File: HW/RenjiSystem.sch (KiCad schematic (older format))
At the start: 35 parts

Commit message: フットプリントをトランス以外あてがい
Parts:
- added C6: CP1, Capacitor_THT:CP_Radial_D12.5mm_P5.00mm, symbol Device:CP1
- added H1: MountingHole_Pad_AC100V_HOT, MountingHole:MountingHole_4.3mm_M4_DIN965_Pad, symbol Mechanical:MountingHole_Pad
- added H2: MountingHole_Pad_FAN_HOT, MountingHole:MountingHole_4.3mm_M4_DIN965_Pad, symbol Mechanical:MountingHole_Pad
- added H3: MountingHole_Pad_HEATER_HOT, MountingHole:MountingHole_4.3mm_M4_DIN965_Pad, symbol Mechanical:MountingHole_Pad
- added H4: MountingHole_Pad_UV_HOT, MountingHole:MountingHole_4.3mm_M4_DIN965_Pad, symbol Mechanical:MountingHole_Pad
- added H5: MountingHole_Pad_UV_COLD, MountingHole:MountingHole_4.3mm_M4_DIN965_Pad, symbol Mechanical:MountingHole_Pad
- added H6: MountingHole_Pad_HEATER_COLD, MountingHole:MountingHole_4.3mm_M4_DIN965_Pad, symbol Mechanical:MountingHole_Pad
- added H7: MountingHole_Pad_FAN_COLD, MountingHole:MountingHole_4.3mm_M4_DIN965_Pad, symbol Mechanical:MountingHole_Pad
- added H8: MountingHole_Pad_AC100V_COLD, MountingHole:MountingHole_4.3mm_M4_DIN965_Pad, symbol Mechanical:MountingHole_Pad
- added RV1: R_POT_US_CONT_ADJUST, Potentiometer_THT:Potentiometer_Bourns_3339P_Vertical_HandSoldering, symbol Device:R_POT_US
- C1, C2, C3, C5: renamed from C?; footprint (none) -> Capacitor_THT:C_Rect_L4.0mm_W2.5mm_P2.50mm
- C4: renamed from C?; footprint (none) -> Capacitor_THT:CP_Radial_D12.5mm_P5.00mm
- D1: renamed from D?; footprint (none) -> Diode_THT:Diode_Bridge_DIP-4_W7.62mm_P5.08mm
- D2, D3, D4: renamed from D?; footprint (none) -> Diode_THT:D_5W_P5.08mm_Vertical_AnodeUp
- J1, J5: renamed from J?; footprint (none) -> Connector_PinSocket_2.54mm:PinSocket_1x03_P2.54mm_Vertical
- J10: renamed from J?; footprint (none) -> Connector_PinHeader_2.54mm:PinHeader_1x05_P2.54mm_Horizontal
- J11, J3, J4, J6: renamed from J?; footprint (none) -> Connector_PinSocket_2.54mm:PinSocket_2x13_P2.54mm_Vertical
- J12: renamed from J?; footprint (none) -> Connector_PinSocket_2.54mm:PinSocket_1x08_P2.54mm_Vertical
- J13: renamed from J?; footprint (none) -> Connector_PinSocket_2.54mm:PinSocket_1x06_P2.54mm_Vertical
- J2, J7: renamed from J?; footprint (none) -> Connector_PinHeader_2.54mm:PinHeader_2x07_P2.54mm_Vertical
- J8, J9: renamed from J?; footprint (none) -> Connector_PinHeader_2.54mm:PinHeader_1x03_P2.54mm_Horizontal
- R1, R2, R3, R4, R5, R6: renamed from R?; footprint (none) -> Resistor_THT:R_Axial_DIN0207_L6.3mm_D2.5mm_P7.62mm_Horizontal
- gave numbers to parts that had none: 7
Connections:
- net labels removed: AC, FAN_CONNECT_COLD, FAN_CONNECT_HOT, HEATER_CONNECT_COLD, HEATER_CONNECT_HOT, UV_CONNECT_COLD, UV_CONNECT_HOT
- wire segments 159 -> 165

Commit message: トランスのフットプリントライブラリ作成
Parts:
- T1: footprint (none) -> Transformer_THT:F24-250-C2
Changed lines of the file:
@@
 F 0 "T1" H 1150 7778 50  0000 C CNN
 F 1 "Transformer_FS24-100-C2" H 1150 7687 50  0000 C CNN
-F 2 "" H 1150 7200 50  0001 C CNN
+F 2 "Transformer_THT:F24-250-C2" H 1150 7200 50  0001 C CNN
 F 3 "~" H 1150 7200 50  0001 C CNN
 	1    1150 7200

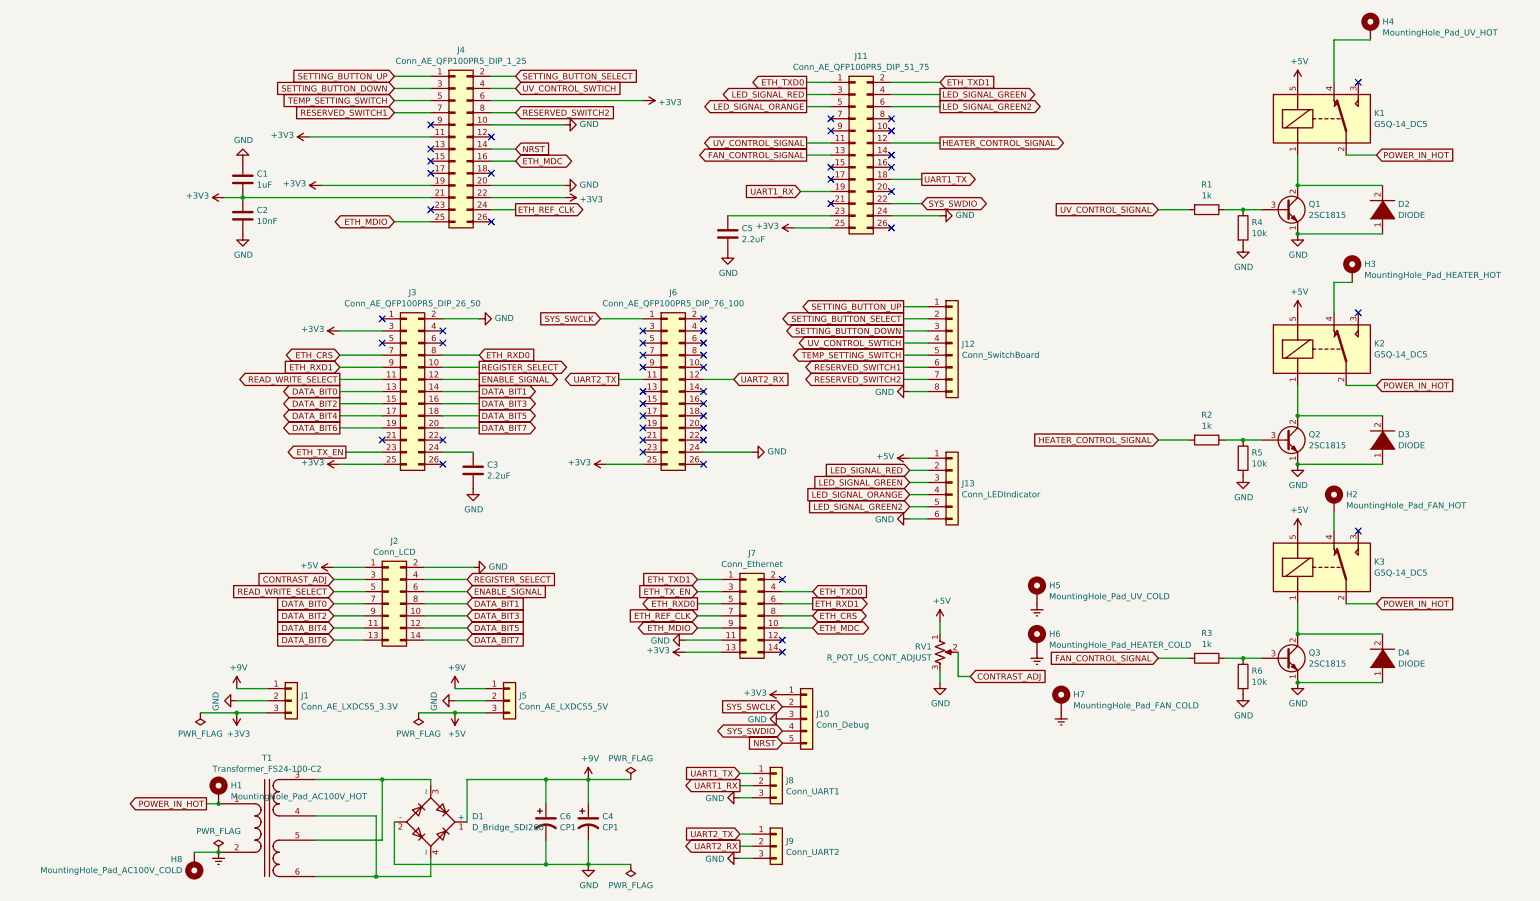
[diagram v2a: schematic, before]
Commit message: ボード回路図を, シート分割
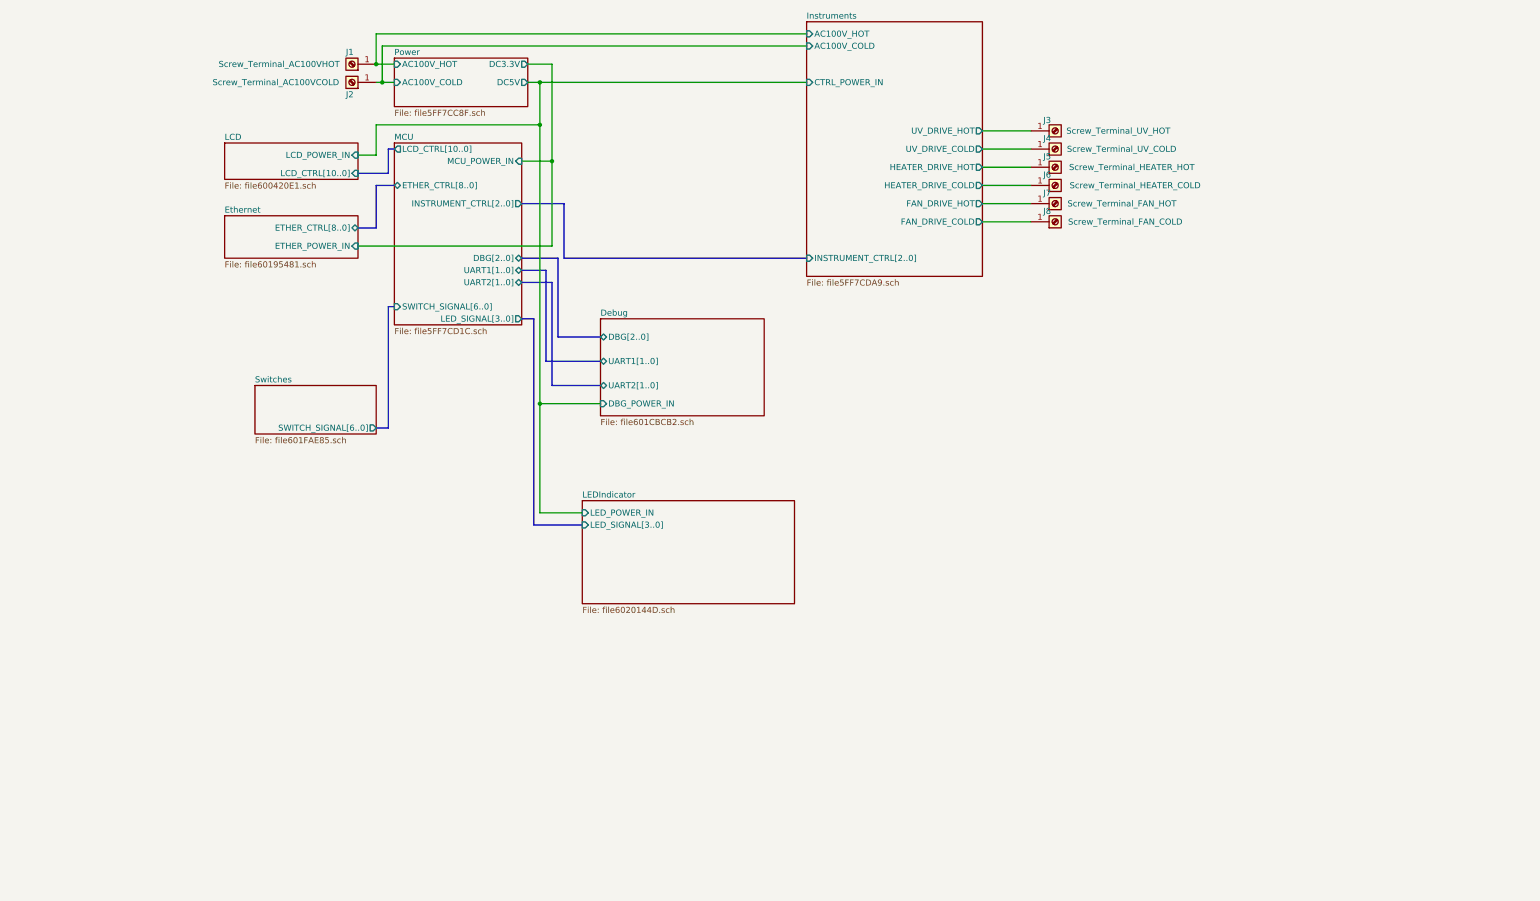
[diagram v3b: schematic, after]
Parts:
- removed C1: 1uF, Capacitor_THT:C_Rect_L4.0mm_W2.5mm_P2.50mm, symbol Device:C
- removed C2: 10nF, Capacitor_THT:C_Rect_L4.0mm_W2.5mm_P2.50mm, symbol Device:C
- removed C3, C5: 2.2uF, Capacitor_THT:C_Rect_L4.0mm_W2.5mm_P2.50mm, symbol Device:C
- removed C4, C6: CP1, Capacitor_THT:CP_Radial_D12.5mm_P5.00mm, symbol Device:CP1
- removed D1: D_Bridge_SDI260, Diode_THT:Diode_Bridge_DIP-4_W7.62mm_P5.08mm, symbol Device:D_Bridge_+-AA
- removed D2, D3, D4: DIODE, Diode_THT:D_5W_P5.08mm_Vertical_AnodeUp, symbol pspice:DIODE
- removed H1: MountingHole_Pad_AC100V_HOT, MountingHole:MountingHole_4.3mm_M4_DIN965_Pad, symbol Mechanical:MountingHole_Pad
- removed H2: MountingHole_Pad_FAN_HOT, MountingHole:MountingHole_4.3mm_M4_DIN965_Pad, symbol Mechanical:MountingHole_Pad
- removed H3: MountingHole_Pad_HEATER_HOT, MountingHole:MountingHole_4.3mm_M4_DIN965_Pad, symbol Mechanical:MountingHole_Pad
- removed H4: MountingHole_Pad_UV_HOT, MountingHole:MountingHole_4.3mm_M4_DIN965_Pad, symbol Mechanical:MountingHole_Pad
- removed H5: MountingHole_Pad_UV_COLD, MountingHole:MountingHole_4.3mm_M4_DIN965_Pad, symbol Mechanical:MountingHole_Pad
- removed H6: MountingHole_Pad_HEATER_COLD, MountingHole:MountingHole_4.3mm_M4_DIN965_Pad, symbol Mechanical:MountingHole_Pad
- removed H7: MountingHole_Pad_FAN_COLD, MountingHole:MountingHole_4.3mm_M4_DIN965_Pad, symbol Mechanical:MountingHole_Pad
- removed H8: MountingHole_Pad_AC100V_COLD, MountingHole:MountingHole_4.3mm_M4_DIN965_Pad, symbol Mechanical:MountingHole_Pad
- removed J1: Conn_AE_LXDC55_3.3V, Connector_PinSocket_2.54mm:PinSocket_1x03_P2.54mm_Vertical, symbol Connector_Generic:Conn_01x03
- removed J10: Conn_Debug, Connector_PinHeader_2.54mm:PinHeader_1x05_P2.54mm_Horizontal, symbol Connector_Generic:Conn_01x05
- removed J11: Conn_AE_QFP100PR5_DIP_51_75, Connector_PinSocket_2.54mm:PinSocket_2x13_P2.54mm_Vertical, symbol Connector_Generic:Conn_02x13_Odd_Even
- removed J12: Conn_SwitchBoard, Connector_PinSocket_2.54mm:PinSocket_1x08_P2.54mm_Vertical, symbol Connector_Generic:Conn_01x08
- removed J13: Conn_LEDIndicator, Connector_PinSocket_2.54mm:PinSocket_1x06_P2.54mm_Vertical, symbol Connector_Generic:Conn_01x06
- removed J2: Conn_LCD, Connector_PinHeader_2.54mm:PinHeader_2x07_P2.54mm_Vertical, symbol Connector_Generic:Conn_02x07_Odd_Even
- removed J3: Conn_AE_QFP100PR5_DIP_26_50, Connector_PinSocket_2.54mm:PinSocket_2x13_P2.54mm_Vertical, symbol Connector_Generic:Conn_02x13_Odd_Even
- removed J4: Conn_AE_QFP100PR5_DIP_1_25, Connector_PinSocket_2.54mm:PinSocket_2x13_P2.54mm_Vertical, symbol Connector_Generic:Conn_02x13_Odd_Even
- removed J5: Conn_AE_LXDC55_5V, Connector_PinSocket_2.54mm:PinSocket_1x03_P2.54mm_Vertical, symbol Connector_Generic:Conn_01x03
- removed J6: Conn_AE_QFP100PR5_DIP_76_100, Connector_PinSocket_2.54mm:PinSocket_2x13_P2.54mm_Vertical, symbol Connector_Generic:Conn_02x13_Odd_Even
- removed J7: Conn_Ethernet, Connector_PinHeader_2.54mm:PinHeader_2x07_P2.54mm_Vertical, symbol Connector_Generic:Conn_02x07_Odd_Even
- removed J8: Conn_UART1, Connector_PinHeader_2.54mm:PinHeader_1x03_P2.54mm_Horizontal, symbol Connector_Generic:Conn_01x03
- removed J9: Conn_UART2, Connector_PinHeader_2.54mm:PinHeader_1x03_P2.54mm_Horizontal, symbol Connector_Generic:Conn_01x03
- removed K1, K2, K3: G5Q-14_DC5, Relay_THT:Relay_SPDT_Omron-G5Q-1, symbol Relay:G5Q-1
- removed Q1, Q2, Q3: 2SC1815, Package_TO_SOT_THT:TO-92_Inline, symbol Transistor_BJT:2SC1815
- removed R1, R2, R3: 1k, Resistor_THT:R_Axial_DIN0207_L6.3mm_D2.5mm_P7.62mm_Horizontal, symbol Device:R
- removed R4, R5, R6: 10k, Resistor_THT:R_Axial_DIN0207_L6.3mm_D2.5mm_P7.62mm_Horizontal, symbol Device:R
- removed RV1: R_POT_US_CONT_ADJUST, Potentiometer_THT:Potentiometer_Bourns_3339P_Vertical_HandSoldering, symbol Device:R_POT_US
- removed T1: Transformer_FS24-100-C2, Transformer_THT:F24-250-C2, symbol Device:Transformer_1P_2S
- added J1: Screw_Terminal_AC100VHOT, symbol Connector:Screw_Terminal_01x01
- added J2: Screw_Terminal_AC100VCOLD, symbol Connector:Screw_Terminal_01x01
- added J3: Screw_Terminal_UV_HOT, symbol Connector:Screw_Terminal_01x01
- added J4: Screw_Terminal_UV_COLD, symbol Connector:Screw_Terminal_01x01
- added J5: Screw_Terminal_HEATER_HOT, symbol Connector:Screw_Terminal_01x01
- added J6: Screw_Terminal_HEATER_COLD, symbol Connector:Screw_Terminal_01x01
- added J7: Screw_Terminal_FAN_HOT, symbol Connector:Screw_Terminal_01x01
- added J8: Screw_Terminal_FAN_COLD, symbol Connector:Screw_Terminal_01x01
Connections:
- new net Instruments/AC100V_COLD: J2.1 (Pin_1)
- new net Instruments/AC100V_HOT: J1.1 (Pin_1)
- new net Instruments/FAN_DRIVE_COLD: J8.1 (Pin_1)
- new net Instruments/FAN_DRIVE_HOT: J7.1 (Pin_1)
- new net Instruments/HEATER_DRIVE_COLD: J6.1 (Pin_1)
- new net Instruments/HEATER_DRIVE_HOT: J5.1 (Pin_1)
- new net Instruments/UV_DRIVE_COLD: J4.1 (Pin_1)
- new net Instruments/UV_DRIVE_HOT: J3.1 (Pin_1)
- no-connect marks 53 -> 0

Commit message: 回路図の配置を修正
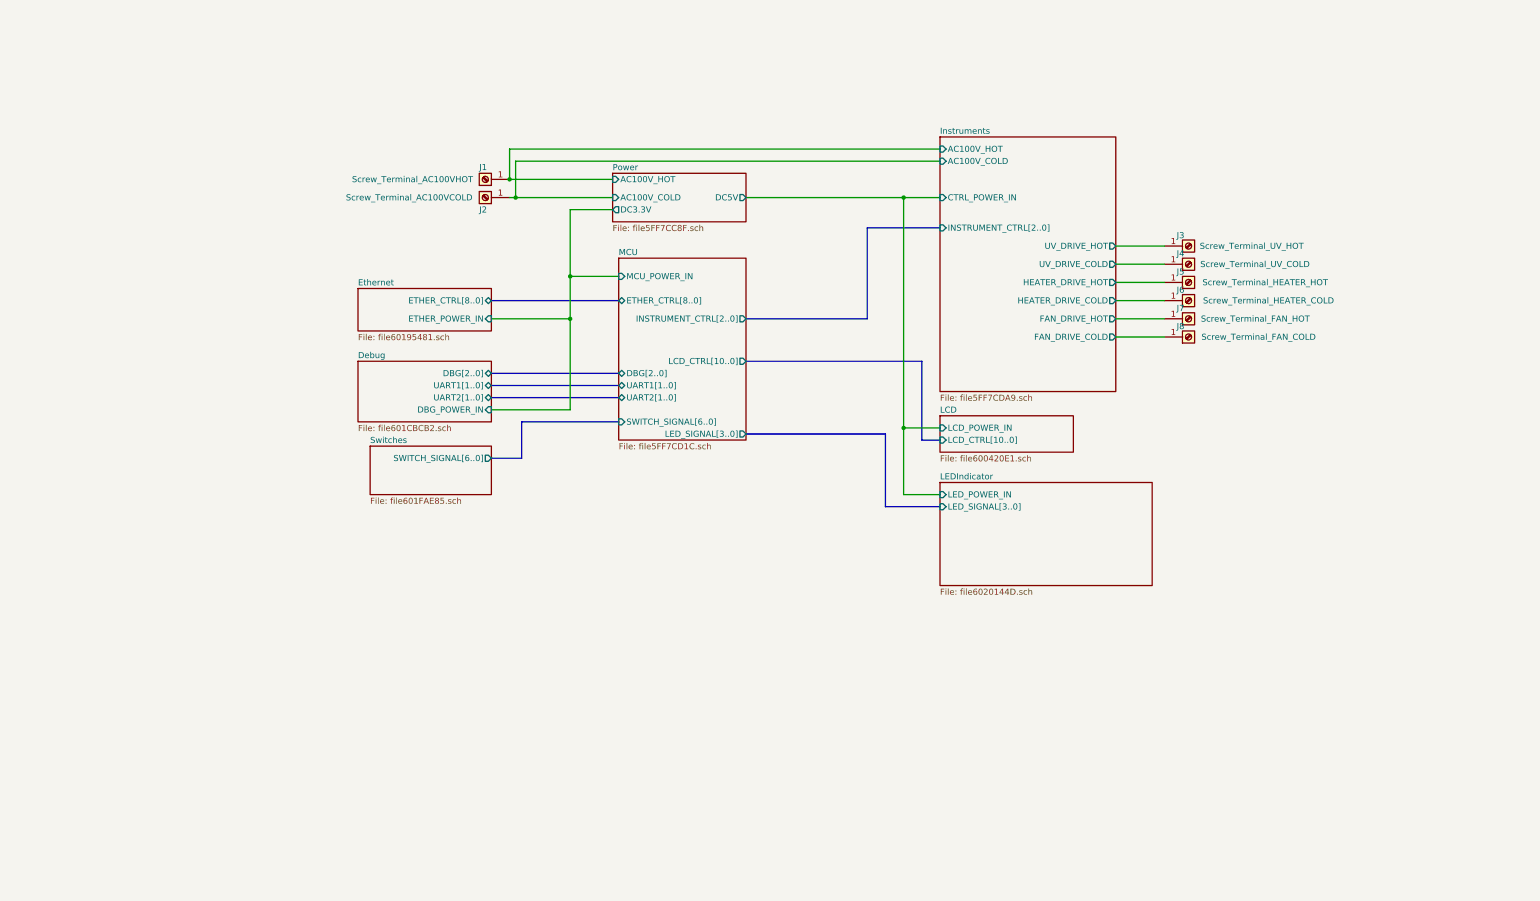
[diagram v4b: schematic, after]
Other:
- moved on the sheet: J1, J2, J3, J4, J5, J6, J7, J8

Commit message: Ethernetボードの配置のためにレイアウト変更
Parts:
- added H1, H2, H3, H4, H5, H6: MountingHole, MountingHole:MountingHole_3.2mm_M3, symbol Mechanical:MountingHole
- J1, J2, J3, J4, J5, J6, J7, J8: footprint (none) -> MyFootPrintLibrary:PCB-20(632)F
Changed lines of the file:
@@
 F 0 "J1" H 3000 1750 50  0000 R CNN
 F 1 "Screw_Terminal_AC100VHOT" H 4050 1850 50  0000 R CNN
-F 2 "" H 2950 1850 50  0001 C CNN
+F 2 "MyFootPrintLibrary:PCB-20(632)F" H 2950 1850 50  0001 C CNN
 F 3 "~" H 2950 1850 50  0001 C CNN
 	1    2950 1850
@@
 F 0 "J2" H 3000 2100 50  0000 R CNN
 F 1 "Screw_Terminal_AC100VCOLD" H 4100 2000 50  0000 R CNN
-F 2 "" H 2950 2000 50  0001 C CNN
+F 2 "MyFootPrintLibrary:PCB-20(632)F" H 2950 2000 50  0001 C CNN
 F 3 "~" H 2950 2000 50  0001 C CNN
 	1    2950 2000
@@
 F 0 "J3" H 8716 2312 50  0000 R CNN
 F 1 "Screw_Terminal_UV_HOT" H 9700 2400 50  0000 R CNN
-F 2 "" H 8750 2400 50  0001 C CNN
+F 2 "MyFootPrintLibrary:PCB-20(632)F" H 8750 2400 50  0001 C CNN
 F 3 "~" H 8750 2400 50  0001 C CNN
 	1    8750 2400
@@
 F 0 "J4" H 8716 2462 50  0000 R CNN
 F 1 "Screw_Terminal_UV_COLD" H 9750 2550 50  0000 R CNN
-F 2 "" H 8750 2550 50  0001 C CNN
+F 2 "MyFootPrintLibrary:PCB-20(632)F" H 8750 2550 50  0001 C CNN
 F 3 "~" H 8750 2550 50  0001 C CNN
 	1    8750 2550
@@
 F 0 "J5" H 8716 2612 50  0000 R CNN
 F 1 "Screw_Terminal_HEATER_HOT" H 9900 2700 50  0000 R CNN
-F 2 "" H 8750 2700 50  0001 C CNN
+F 2 "MyFootPrintLibrary:PCB-20(632)F" H 8750 2700 50  0001 C CNN
 F 3 "~" H 8750 2700 50  0001 C CNN
 	1    8750 2700
@@
 F 0 "J6" H 8716 2762 50  0000 R CNN
 F 1 "Screw_Terminal_HEATER_COLD" H 9950 2850 50  0000 R CNN
-F 2 "" H 8750 2850 50  0001 C CNN
+F 2 "MyFootPrintLibrary:PCB-20(632)F" H 8750 2850 50  0001 C CNN
 F 3 "~" H 8750 2850 50  0001 C CNN
 	1    8750 2850
@@
 F 0 "J7" H 8716 2912 50  0000 R CNN
 F 1 "Screw_Terminal_FAN_HOT" H 9750 3000 50  0000 R CNN
-F 2 "" H 8750 3000 50  0001 C CNN
+F 2 "MyFootPrintLibrary:PCB-20(632)F" H 8750 3000 50  0001 C CNN
 F 3 "~" H 8750 3000 50  0001 C CNN
 	1    8750 3000
@@
 F 0 "J8" H 8716 3062 50  0000 R CNN
 F 1 "Screw_Terminal_FAN_COLD" H 9800 3150 50  0000 R CNN
-F 2 "" H 8750 3150 50  0001 C CNN
+F 2 "MyFootPrintLibrary:PCB-20(632)F" H 8750 3150 50  0001 C CNN
 F 3 "~" H 8750 3150 50  0001 C CNN
 	1    8750 3150
@@
 Wire Bus Line
 	3250 4150 3000 4150
+$Comp
+L Mechanical:MountingHole H1
+U 1 1 602F013A
+P 1100 900
+F 0 "H1" H 1200 946 50  0000 L CNN
+F 1 "MountingHole" H 1200 855 50  0000 L CNN
+F 2 "MountingHole:MountingHole_3.2mm_M3" H 1100 900 50  0001 C CNN
+F 3 "~" H 1100 900 50  0001 C CNN
+	1    1100 900
+	1    0    0    -1
+$EndComp
+$Comp
+L Mechanical:MountingHole H3
+U 1 1 602F01B4
+P 10250 850
+F 0 "H3" H 10350 896 50  0000 L CNN
+F 1 "MountingHole" H 10350 805 50  0000 L CNN
+F 2 "MountingHole:MountingHole_3.2mm_M3" H 10250 850 50  0001 C CNN
+F 3 "~" H 10250 850 50  0001 C CNN
+	1    10250 850
+	1    0    0    -1
+$EndComp
+$Comp
+L Mechanical:MountingHole H2
+U 1 1 602F034D
+P 1300 5300
+F 0 "H2" H 1400 5346 50  0000 L CNN
+F 1 "MountingHole" H 1400 5255 50  0000 L CNN
+F 2 "MountingHole:MountingHole_3.2mm_M3" H 1300 5300 50  0001 C CNN
+F 3 "~" H 1300 5300 50  0001 C CNN
+	1    1300 5300
+	1    0    0    -1
+$EndComp
+$Comp
+L Mechanical:MountingHole H4
+U 1 1 602F03DD
+P 10350 5200
+F 0 "H4" H 10450 5246 50  0000 L CNN
+F 1 "MountingHole" H 10450 5155 50  0000 L CNN
+F 2 "MountingHole:MountingHole_3.2mm_M3" H 10350 5200 50  0001 C CNN
+F 3 "~" H 10350 5200 50  0001 C CNN
+	1    10350 5200
+	1    0    0    -1
+$EndComp
+$Comp
+L Mechanical:MountingHole H5
+U 1 1 60352EDE
+P 5250 5300
+F 0 "H5" H 5350 5346 50  0000 L CNN
+F 1 "MountingHole" H 5350 5255 50  0000 L CNN
+F 2 "MountingHole:MountingHole_3.2mm_M3" H 5250 5300 50  0001 C CNN
+F 3 "~" H 5250 5300 50  0001 C CNN
+	1    5250 5300
+	1    0    0    -1
+$EndComp
+$Comp
+L Mechanical:MountingHole H6
+U 1 1 60352F59
+P 6150 5250
+F 0 "H6" H 6250 5296 50  0000 L CNN
+F 1 "MountingHole" H 6250 5205 50  0000 L CNN
+F 2 "MountingHole:MountingHole_3.2mm_M3" H 6150 5250 50  0001 C CNN
+F 3 "~" H 6150 5250 50  0001 C CNN
+	1    6150 5250
+	1    0    0    -1
+$EndComp
 $EndSCHEMATC
